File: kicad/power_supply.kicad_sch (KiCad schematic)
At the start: 12 parts, among them U1 TPS560430X

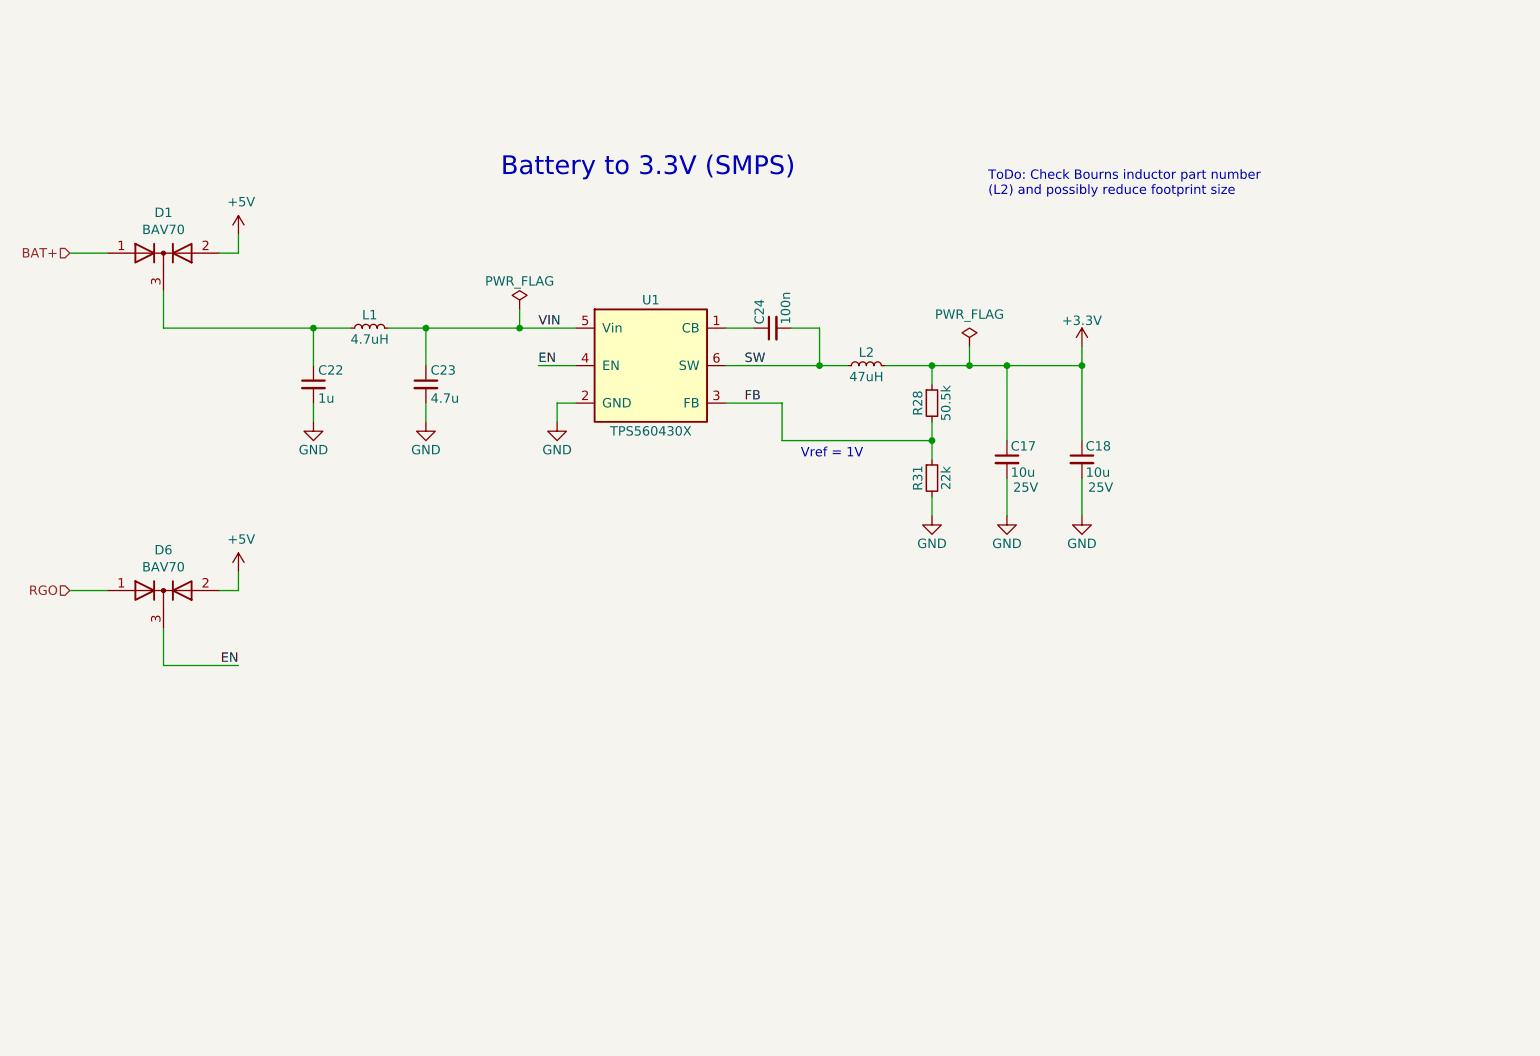
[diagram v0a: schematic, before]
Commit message: WIP: Schematic almost finished
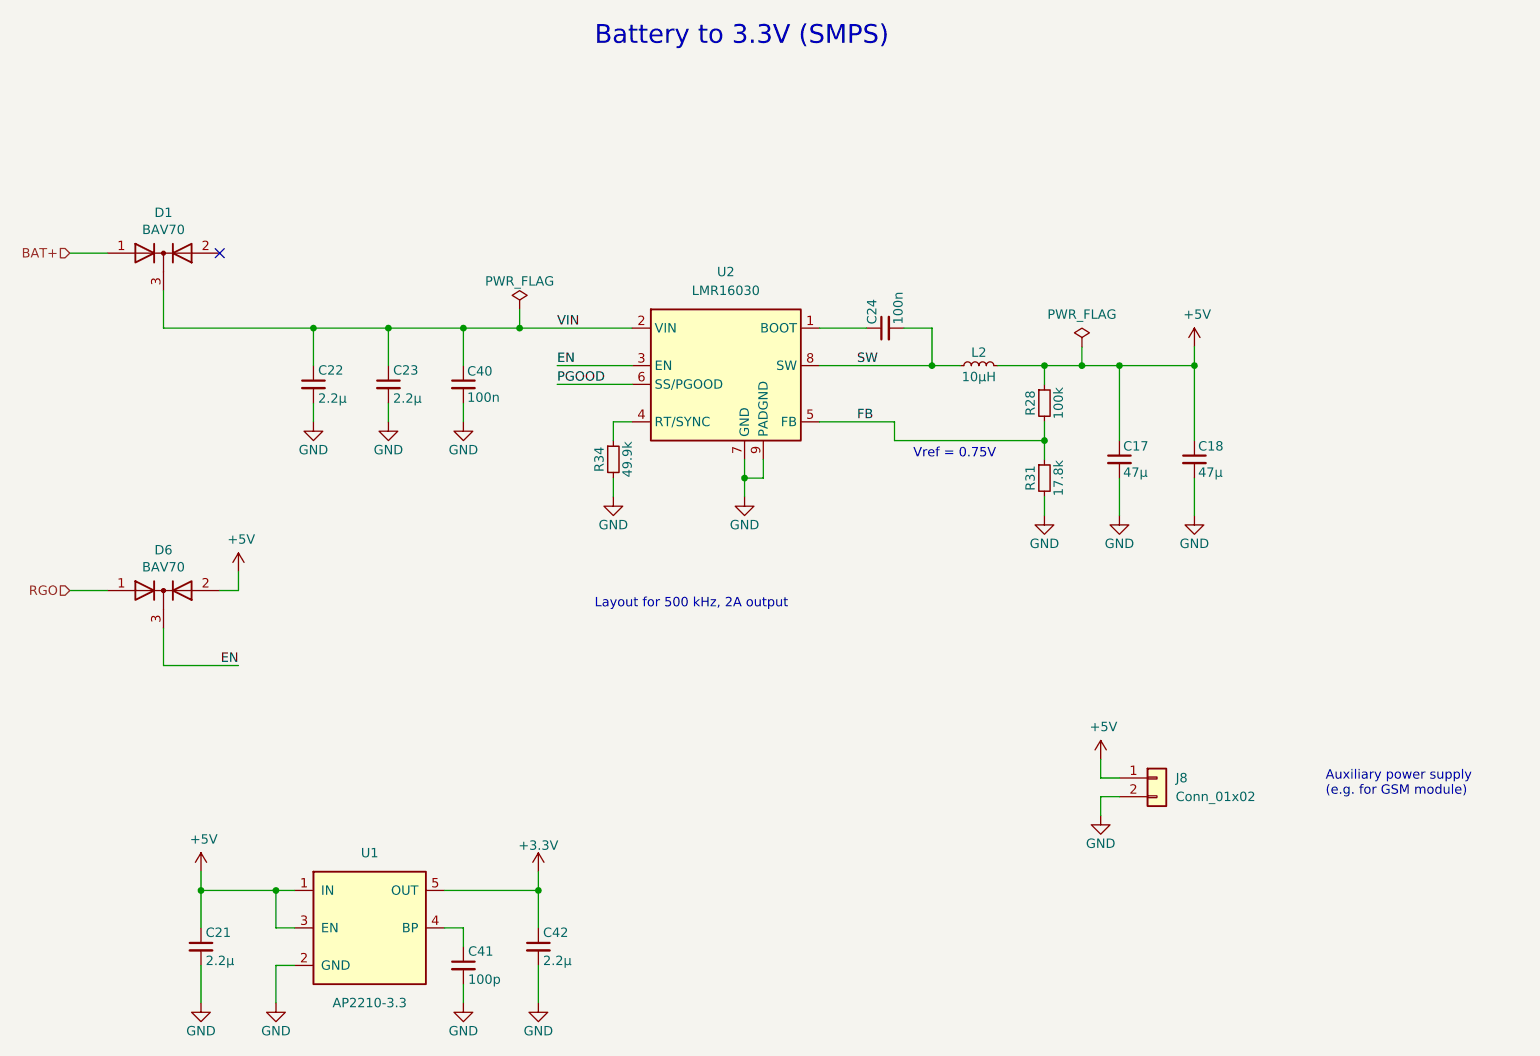
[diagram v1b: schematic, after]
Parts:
- removed L1: 4.7uH, Inductor_SMD:L_0805_2012Metric, symbol Device:L_Small
- removed U1: TPS560430X, LibreSolar:SOT-23-6, symbol LibreSolar:LMR16006
- added C21, C42: 2.2µ, LibreSolar:C_0805_2012, symbol LibreSolar:C
- added C40: 100n, LibreSolar:C_0603_1608, symbol LibreSolar:C
- added C41: 100p, LibreSolar:C_0603_1608, symbol LibreSolar:C
- added J8: Conn_01x02, Connector_JST:JST_PH_B2B-PH-K_1x02_P2.00mm_Vertical, symbol Connector_Generic:Conn_01x02
- added R34: 49.9k, LibreSolar:R_0603_1608, symbol LibreSolar:R
- added U1: AP2210-3.3, Package_TO_SOT_SMD:SOT-23-5, symbol LibreSolar:AP2210-3.3
- added U2: LMR16030, Package_SO:SOIC-8-1EP_3.9x4.9mm_P1.27mm_EP2.29x3mm, symbol LibreSolar:LMR16030
- C17, C18: value 10u -> 47µ; footprint LibreSolar:C_0805_2012 -> LibreSolar:C_1210_3225; Manufacturer Murata -> Samsung; PartNumber GRM21BR61E106KA73L -> CL32B476MPJNNNE; Remarks 25V -> 10V, X5R
- C22: value 1u -> 2.2µ; footprint LibreSolar:C_0603_1608 -> LibreSolar:C_1210_3225; Manufacturer Murata -> (none); PartNumber GRT188R61H105KE13D -> (none); Remarks 50V, X5R -> 100V, X7R
- C23: value 4.7u -> 2.2µ; Manufacturer Murata -> (none); PartNumber GRM31CR71H475MA12L -> (none); Remarks (none) -> 100V, X7R
- L2: value 47uH -> 10µH; footprint LibreSolar:Bourns_SRN6045TA -> LibreSolar:Bourns_SRN8040TA; PartNumber NR6045T470M -> NR8040T100M; Remarks Alternative: Bourns SRR6045TA-470Y -> Alternative: Bourns SRN8040TA-100M
- R28: value 50.5k -> 100k; Manufacturer Yageo -> any; PartNumber RC0603FR-0750K5L -> (none)
- R31: value 22k -> 17.8k; Manufacturer Yageo -> any; PartNumber RC0603FR-0722KL -> (none)
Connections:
- net +3V3: now also C42.1, U1.5 (OUT); no longer C17.1, C18.1, L2.2, R28.1
- net +5V: now also C17.1, C18.1, L2.2, R28.1, C21.1, J8.1 (Pin_1), U1.1 (IN), U1.3 (EN); no longer D1.2 (A)
- net EN: now also U2.3 (EN)
- net FB: now also U2.5 (FB)
- net GND: now also C21.2, C40.2, C41.2, C42.2, J8.2 (Pin_2), R34.2, U1.2 (GND), U2.7 (GND), U2.9 (PADGND)
- net SW: now also U2.8 (SW)
- net VIN: now also C22.1, D1.3 (K), C40.1, U2.2 (VIN)
- net at C24.1: now also U2.1 (BOOT)
- new net: C41.1, U1.4 (BP)
- new net: R34.1, U2.4 (RT/SYNC)
- new net PGOOD: U2.6 (SS/PGOOD)
- no-connect marks 0 -> 1
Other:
- note added: "Auxiliary power supply (e.g. for GSM module)"
- note added: "Layout for 500 kHz, 2A output"
- note added: "Vref = 0.75V"
- note removed: "ToDo: Check Bourns inductor part number (L2) and possibly reduce footprint size"
- note removed: "Vref = 1V"
- title: BMS 8S50 IC -> BMS 16S Control Board
- moved on the sheet: C17, C18, C23, C24, L2, R28, R31

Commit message: v0.1 design ready for review
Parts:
- removed D1, D6: BAV70, LibreSolar:SOT-23, symbol Diode:BAV70
- added D1: 100V, Diode_SMD:D_SOD-123, symbol LibreSolar:D_Schottky
- added D9: D_Schottky, Diode_SMD:D_SOD-128, symbol LibreSolar:D_Schottky
- added R25: 1M, LibreSolar:R_0603_1608, symbol LibreSolar:R
- C17, C18: value 47µ -> 47µF
- C21, C22, C23, C42: value 2.2µ -> 2.2µF
- C24: value 100n -> 100nF; Manufacturer Yageo -> any; PartNumber CC0603KRX7R9BB104 -> (none)
- C40: value 100n -> 100nF; Manufacturer (none) -> any
- C41: value 100p -> 100pF; Manufacturer (none) -> any; Remarks (none) -> 100V, C0G/NP0
- R28, R31, R34: Remarks (none) -> 1%
- U2: Remarks (none) -> Better alternative: LMR38020 (NOT pin-compatible!)
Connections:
- net BAT+: now also D1.2 (A)
- net EN: now also R25.2
- net GND: now also D9.2 (A)
- net SW: now also D9.1 (K)
- net VIN: now also D1.1 (K), R25.1
- no-connect marks 1 -> 0
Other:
- note added: "Pull-up for testing purposes"
- note added: "Remark: LMR38020 is a more suitable alternative for the LMR16030, but it was not available as of 02/2022 due to chip crisis."
- moved on the sheet: C22, C23, C40

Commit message: Updates based on review comments (v0.2)
This is the design revision that was ordered for the first prototype build.

The pinout of the cell connector and the board-to-board connector changed
compared to v0.1, hence it got a minor revision update.

The control board is now a 4-layer board to improve the grounding of the
PCB. Various other suggested improvements from the design review are also
included in this update.

Fixes #11, #12, #13, #17, #18, #19
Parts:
- C21, C42: footprint LibreSolar:C_0805_2012 -> LibreSolar:C_0603_1608; Manufacturer (none) -> any; Remarks (none) -> X7R, 10V
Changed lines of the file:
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@@
   (title_block
     (title "BMS 16S Control Board")
-    (date "2022-02-24")
-    (rev "0.1")
+    (date "2022-03-15")
+    (rev "0.2")
     (company "Libre Solar Technologies GmbH")
     (comment 1 "Website: https://libre.solar")
@@
       (effects (font (size 1.27 1.27)) (justify left))
     )
-    (property "Footprint" "LibreSolar:C_0805_2012" (id 2) (at 76.2 165.1 0)
+    (property "Footprint" "LibreSolar:C_0603_1608" (id 2) (at 76.2 165.1 0)
       (effects (font (size 1.27 1.27)) hide)
     )
     (property "Datasheet" "" (id 3) (at 76.835 158.115 0))
+    (property "Manufacturer" "any" (id 4) (at 76.2 160.02 0)
+      (effects (font (size 1.27 1.27)) hide)
+    )
+    (property "Remarks" "X7R, 10V" (id 5) (at 76.2 160.02 0)
+      (effects (font (size 1.27 1.27)) hide)
+    )
     (pin "1")
     (pin "2")
@@
       (effects (font (size 1.27 1.27)) (justify left))
     )
-    (property "Footprint" "LibreSolar:C_0805_2012" (id 2) (at 121.92 165.1 0)
+    (property "Footprint" "LibreSolar:C_0603_1608" (id 2) (at 121.92 165.1 0)
       (effects (font (size 1.27 1.27)) hide)
     )
     (property "Datasheet" "" (id 3) (at 122.555 158.115 0))
-    (pin "1")
-    (pin "2")
+    (property "Manufacturer" "any" (id 4) (at 121.92 160.02 0)
+      (effects (font (size 1.27 1.27)) hide)
+    )
+    (property "Remarks" "X7R, 10V" (id 5) (at 121.92 160.02 0)
+      (effects (font (size 1.27 1.27)) hide)
+    )
+    (pin "1")
+    (pin "2")

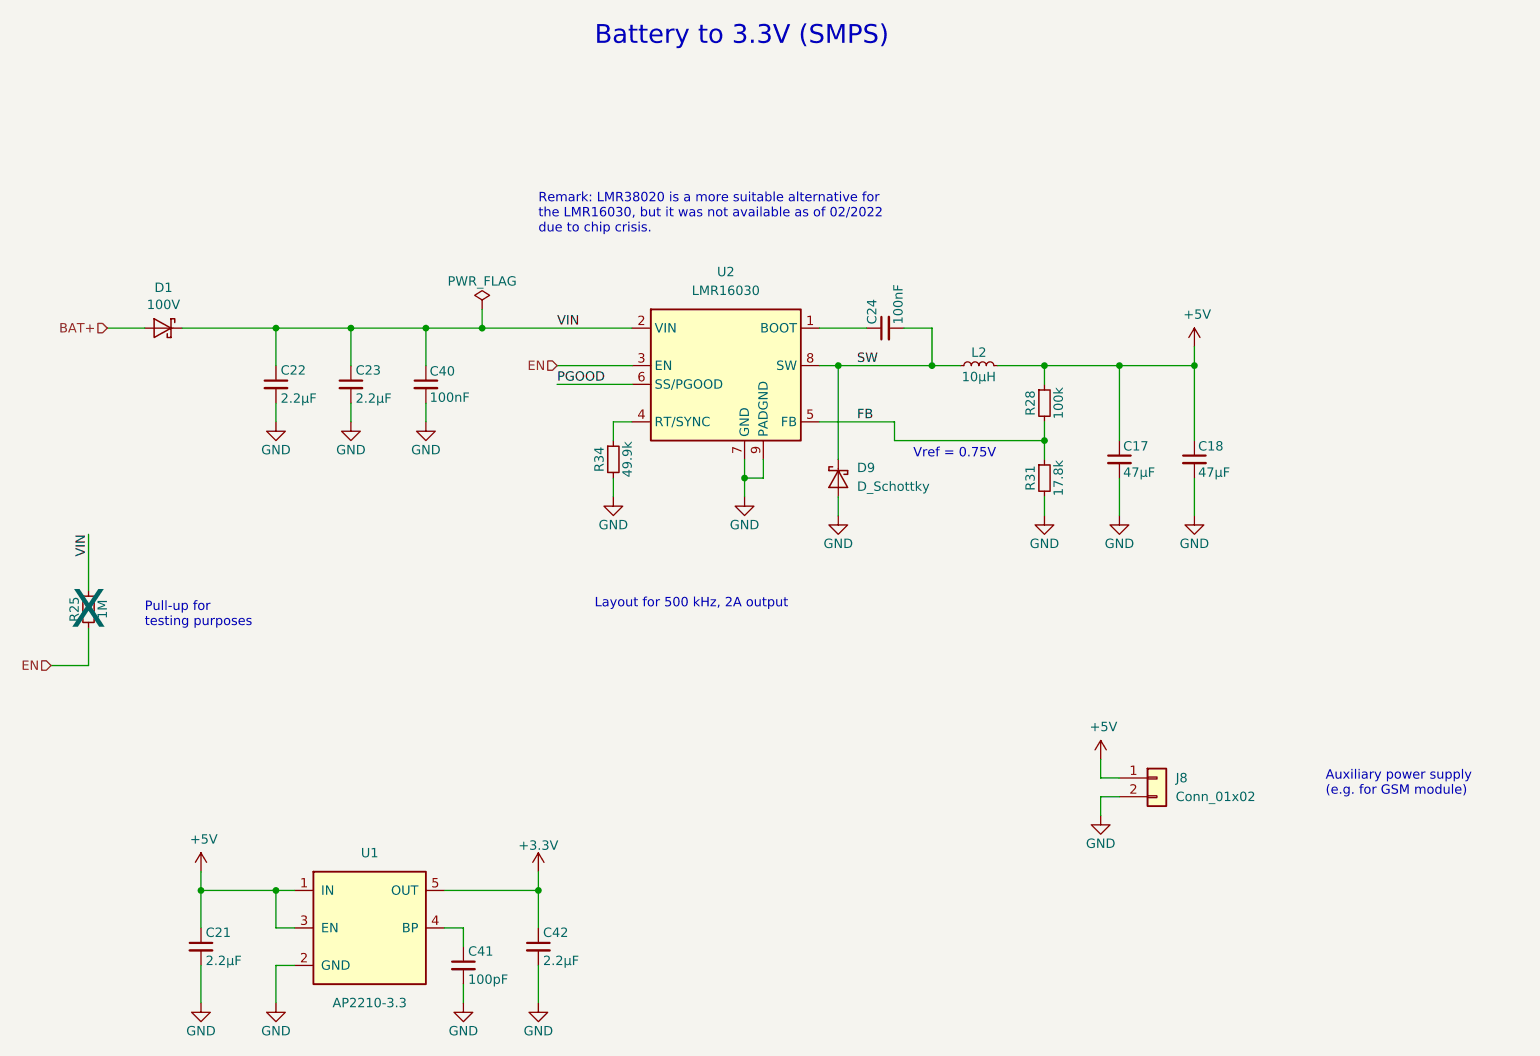
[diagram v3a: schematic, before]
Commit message: Major update for BMS C1 v0.3
This commit contains major updates of the PCB after the first prototype
build-up and testing. Changes include:

- Single PCB instead of stacked PCBs to simplify design and reduce cost.
- STM32 MCU was removed due to supply shortage. Only ESP32-C3 supported.
- Custom connectors replaced with off-the-shelf Würth Power Elements.
- 5V power rail removed to simplify design (CAN runs on 3V3 transceiver).
- Larger Shunt with improved footprint.
- Optimized layout to reduce distance between IC and shunt.
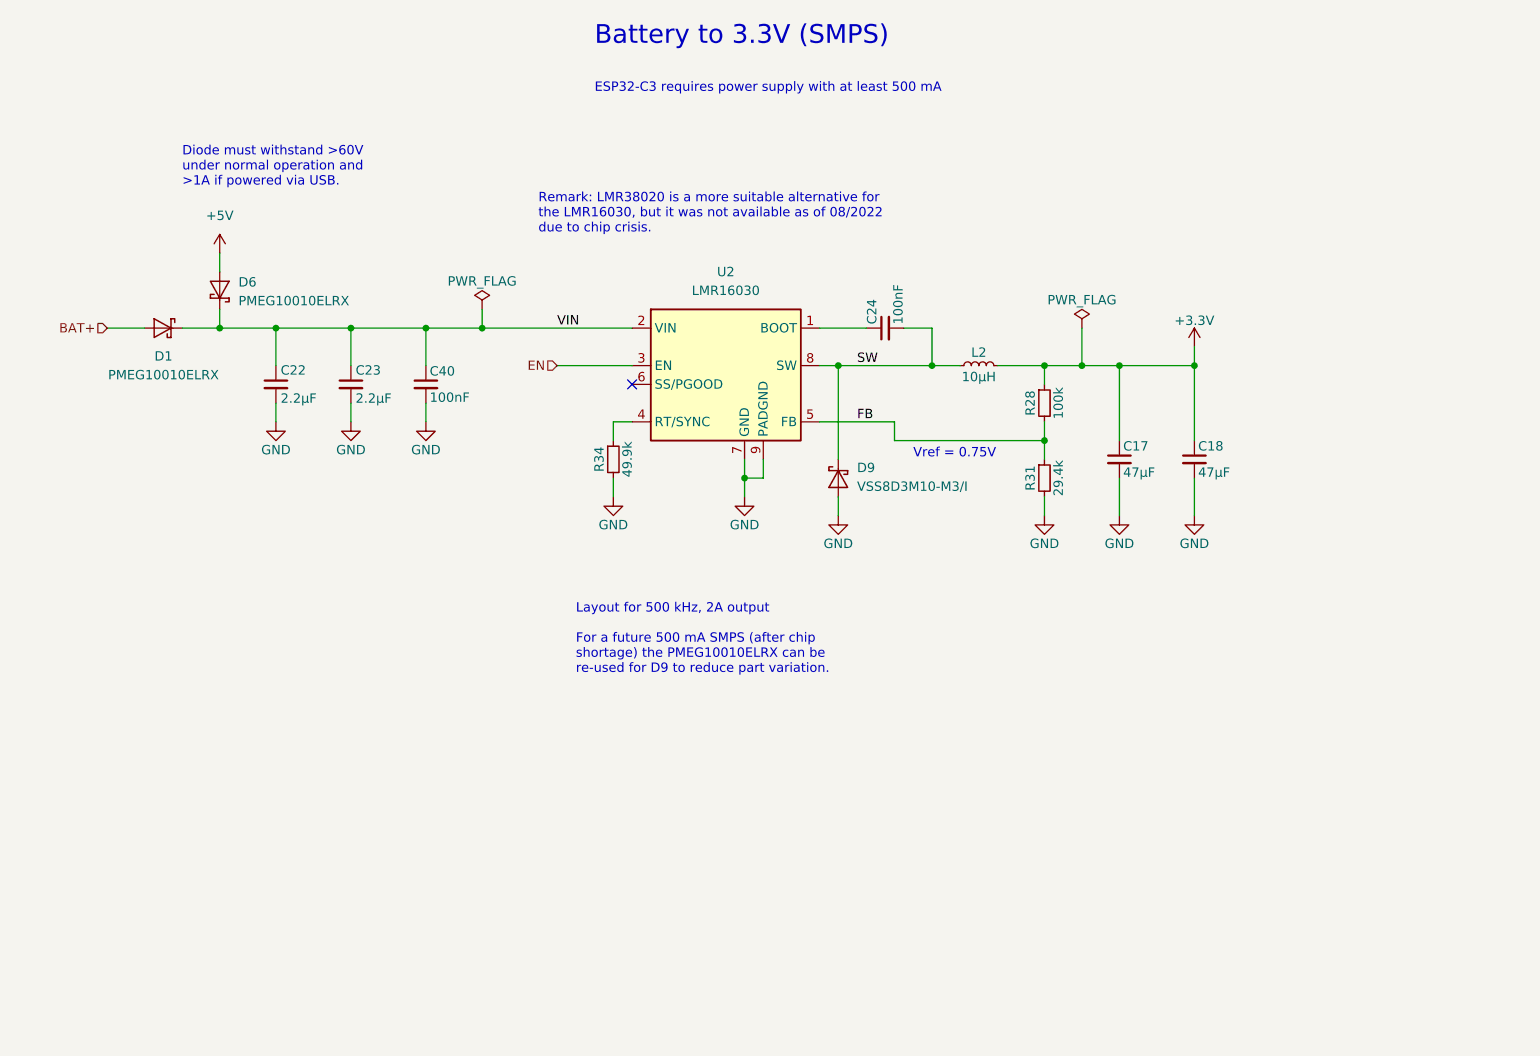
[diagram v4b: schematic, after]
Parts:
- removed C21, C42: 2.2µF, LibreSolar:C_0603_1608, symbol LibreSolar:C
- removed C41: 100pF, LibreSolar:C_0603_1608, symbol LibreSolar:C
- removed J8: Conn_01x02, Connector_JST:JST_PH_B2B-PH-K_1x02_P2.00mm_Vertical, symbol Connector_Generic:Conn_01x02
- removed R25: 1M, LibreSolar:R_0603_1608, symbol LibreSolar:R
- removed U1: AP2210-3.3, Package_TO_SOT_SMD:SOT-23-5, symbol LibreSolar:AP2210-3.3
- added D6: PMEG10010ELRX, LibreSolar:D_SOD-123F, symbol LibreSolar:D_Schottky
- C22, C23: Manufacturer (none) -> any
- C24: Remarks (none) -> X7R, 100V
- C40: Remarks 100V -> X7R, 100V
- D1: value 100V -> PMEG10010ELRX; footprint Diode_SMD:D_SOD-123 -> LibreSolar:D_SOD-123F; Manufacturer Diodes Incorporated -> Vishay; PartNumber BAT46W-7-F -> PMEG10010ELRX; Remarks (none) -> Alternative: Nexperia PMEG10030ELPX
- D9: value D_Schottky -> VSS8D3M10-M3/I
- R31: value 17.8k -> 29.4k
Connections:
- net +3V3: now also C17.1, C18.1, L2.2, R28.1
- net +5V: now also D6.2 (A); no longer C17.1, C18.1, L2.2, R28.1
- net VIN: now also D6.1 (K)
- net PGOOD: no longer names the net of U2.6 (SS/PGOOD)
- no-connect marks 0 -> 1
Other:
- note added: "Diode must withstand >60V under normal operation and >1A if powered via USB."
- note added: "ESP32-C3 requires power supply with at least 500 mA"
- note added: "Layout for 500 kHz, 2A output For a future 500 mA SMPS (after chip shortage) the PMEG10010ELRX can be re-used for D9 to reduce part variation."
- note added: "Remark: LMR38020 is a more suitable alternative for the LMR16030, but it was not available as of 08/2022 due to chip crisis."
- note removed: "Auxiliary power supply (e.g. for GSM module)"
- note removed: "Layout for 500 kHz, 2A output"
- note removed: "Pull-up for testing purposes"
- note removed: "Remark: LMR38020 is a more suitable alternative for the LMR16030, but it was not available as of 02/2022 due to chip crisis."
- title: BMS 16S Control Board -> Libre Solar BMS C1

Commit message: BOM updates with a few more alternative parts
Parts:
- D1, D6: Manufacturer Vishay -> Nexperia
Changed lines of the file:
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@@
       (effects (font (size 1.27 1.27)) hide)
     )
-    (property "Manufacturer" "Vishay" (id 4) (at 78.74 71.12 0)
+    (property "Manufacturer" "Nexperia" (id 4) (at 78.74 71.12 0)
       (effects (font (size 1.27 1.27)) hide)
     )
@@
       (effects (font (size 1.27 1.27)) hide)
     )
-    (property "Manufacturer" "Vishay" (id 4) (at 71.12 76.2 0)
+    (property "Manufacturer" "Nexperia" (id 4) (at 71.12 76.2 0)
       (effects (font (size 1.27 1.27)) hide)
     )
